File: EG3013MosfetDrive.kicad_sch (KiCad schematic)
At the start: 32 parts, among them J1 Conn_02x03_Odd_Even, Q1 QM6006D, Q2 QM6006D, Q3 QM6006D, Q4 QM6006D, U1 EG3013, U2 EG3013

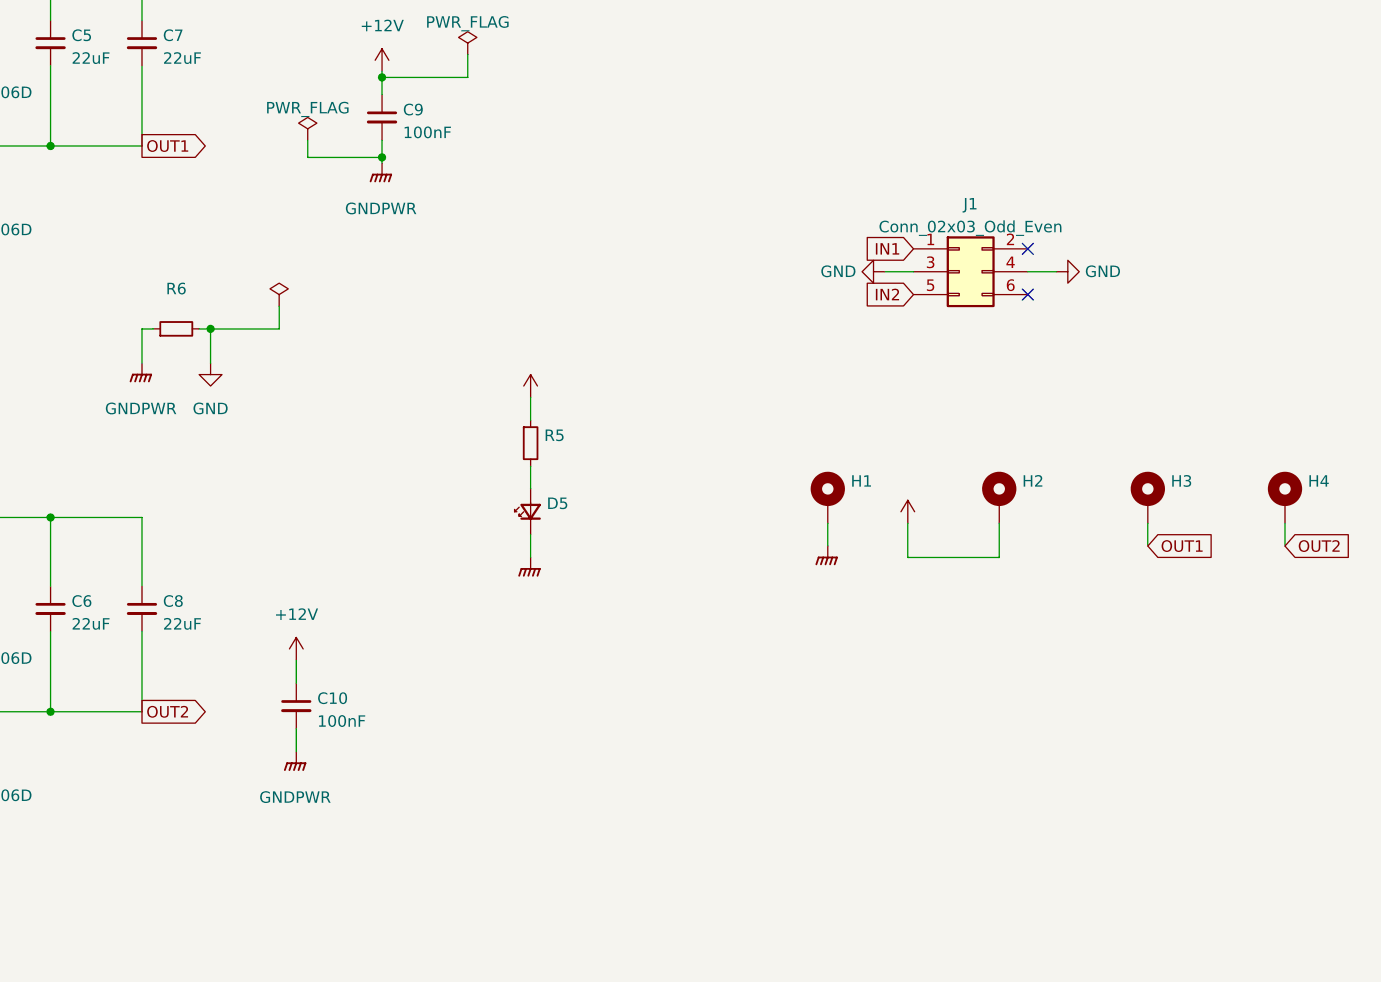
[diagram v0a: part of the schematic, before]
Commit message: PWM端口添加下拉电阻
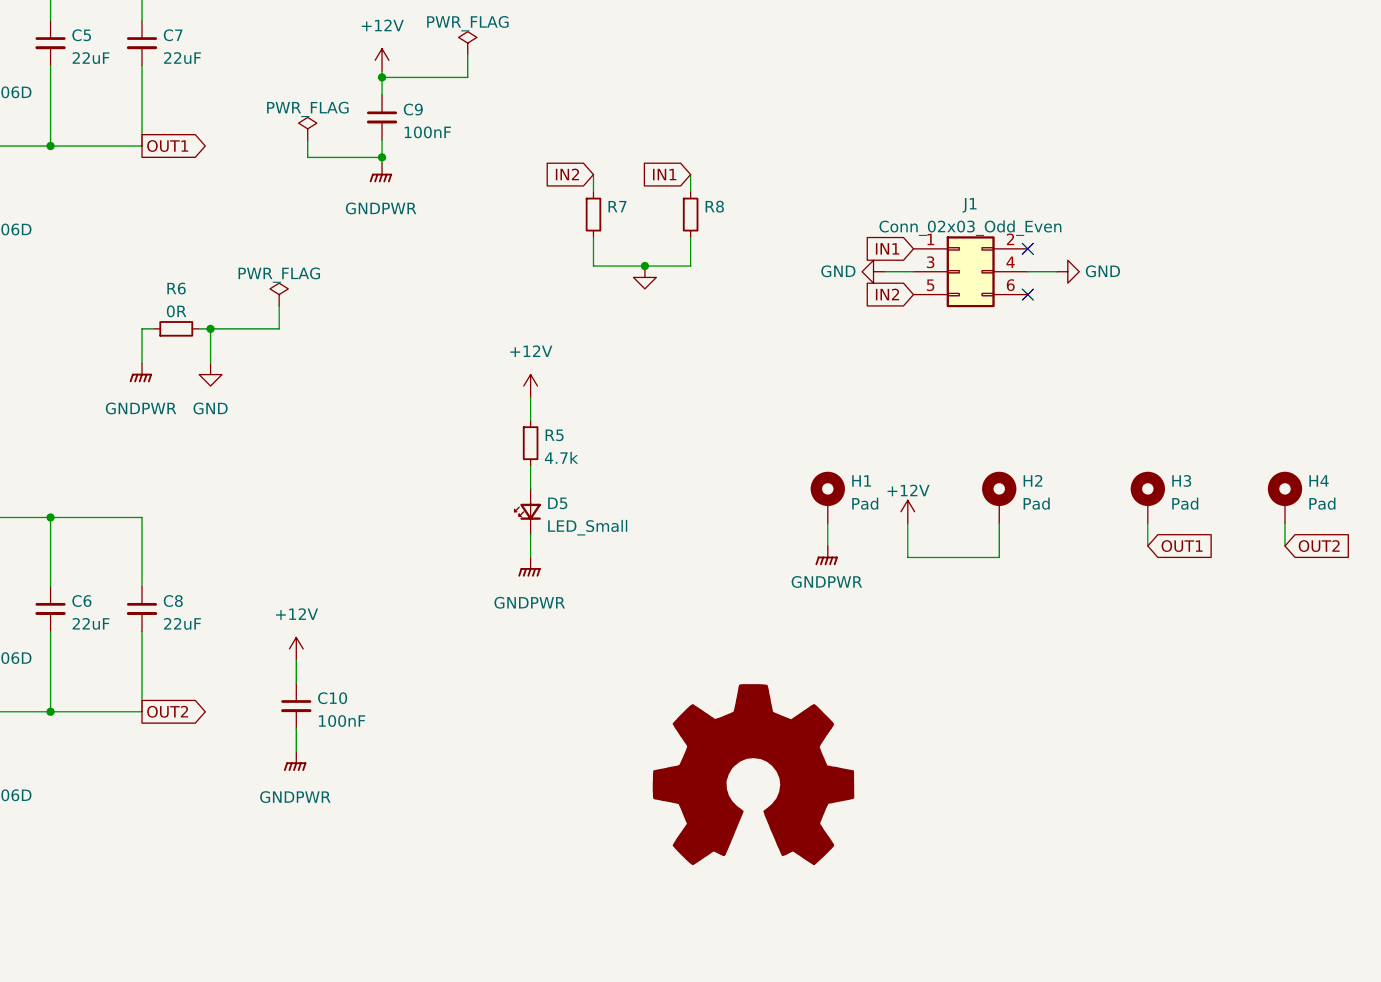
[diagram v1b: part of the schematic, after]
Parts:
- added R7, R8: (no value), symbol Device:R_Small
- D5: value (none) -> LED_Small; footprint (none) -> LED_SMD:LED_0402_1005Metric
- H1, H2, H3, H4: value (none) -> Pad; footprint (none) -> MountingHole:MountingHole_2.5mm_Pad_Via
- J1: footprint (none) -> Connector_IDC:IDC-Header_2x03_P2.54mm_Vertical
- R5: value (none) -> 4.7k; footprint (none) -> Resistor_SMD:R_0402_1005Metric
- R6: value (none) -> 0R; footprint (none) -> Resistor_SMD:R_0603_1608Metric
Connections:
- net GND: now also R7.2, R8.2
- net IN1: now also R8.1
- net IN2: now also R7.1

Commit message: fix some net
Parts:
- R7, R8: value (none) -> 1k; footprint (none) -> Resistor_SMD:R_0402_1005Metric
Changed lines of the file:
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@@
       (effects (font (size 1.27 1.27)) hide)
     )
-    (property "Value" "" (id 1) (at 188.595 154.94 0)
+    (property "Value" "Logo_Open_Hardware_Large" (id 1) (at 188.595 154.94 0)
       (effects (font (size 1.27 1.27)) hide)
     )
@@
       (effects (font (size 1.27 1.27)) (justify left))
     )
-    (property "Value" "" (id 1) (at 172.3136 82.9822 0)
-      (effects (font (size 1.27 1.27)) (justify left))
-    )
-    (property "Footprint" "" (id 2) (at 170.815 81.28 0)
+    (property "Value" "1k" (id 1) (at 172.3136 82.9822 0)
+      (effects (font (size 1.27 1.27)) (justify left))
+    )
+    (property "Footprint" "Resistor_SMD:R_0402_1005Metric" (id 2) (at 170.815 81.28 0)
       (effects (font (size 1.27 1.27)) hide)
     )
@@
       (effects (font (size 1.27 1.27)) hide)
     )
-    (property "Value" "" (id 1) (at 178.435 88.6988 0)
+    (property "Value" "GND" (id 1) (at 178.435 88.6988 0)
       (effects (font (size 1.27 1.27)) (justify left))
     )
@@
       (effects (font (size 1.27 1.27)) (justify left))
     )
-    (property "Value" "" (id 1) (at 183.1086 82.9822 0)
-      (effects (font (size 1.27 1.27)) (justify left))
-    )
-    (property "Footprint" "" (id 2) (at 181.61 81.28 0)
-      (effects (font (size 1.27 1.27)) hide)
-    )
+    (property "Value" "1k" (id 1) (at 183.1086 82.9822 0)
+      (effects (font (size 1.27 1.27)) (justify left))
+    )
+    (property "Footprint" "Resistor_SMD:R_0402_1005Metric" (id 2) (at 181.61 81.28 0)
+      (effects (font (size 1.27 1.27)) hide)
+    )

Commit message: model D Vesion
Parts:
- added C11, C12: 100nF, Capacitor_SMD:C_0603_1608Metric, symbol Device:C_Small
- added C13, C14, C15, C16: 10nF, Capacitor_SMD:C_0402_1005Metric, symbol Device:C_Small
- added C17, C18, C19, C20: 22uF, Capacitor_SMD:C_0603_1608Metric, symbol Device:C_Small
- added D6, D7, D8, D9: 1N4148, Diode_SMD:D_SOD-123, symbol Device:D_Small
- added H3, H6: Pad, MountingHole:MountingHole_2.5mm_Pad_Via, symbol Mechanical:MountingHole_Pad
- added Q5, Q6, Q7, Q8: QM6006D, Package_TO_SOT_SMD:TO-252-2, symbol Transistor_FET:QM6006D
- added R10, R9: 1k, Resistor_SMD:R_0402_1005Metric, symbol Device:R_Small
- added R11, R12, R13, R14: 22R, Resistor_SMD:R_0402_1005Metric, symbol Device:R_Small
- added U3, U4: EG3013, Package_SO:SOIC-8_3.9x4.9mm_P1.27mm, symbol Driver_FET:IR2103
- renumbered C10 to C1, C8 to C10, C9 to C2, C1 to C3, C2 to C4, C3 to C5, C4 to C6, C5 to C7, C6 to C8, C7 to C9, D5 to D1, D1 to D2, D2 to D3, D3 to D4, D4 to D5, H3 to H2, H2 to H4, H4 to H5, R6 to R1, R5 to R2, R1 to R3, R2 to R4, R3 to R5, R4 to R6
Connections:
- net +12V: now also C11.1, C12.1, Q5.2 (D), Q7.2 (D), U3.1 (VCC), U4.1 (VCC)
- net GND: now also R10.2, R9.2
- net GNDPWR: now also C11.2, C12.2, C14.1, C16.1, Q6.3 (S), Q8.3 (S), U3.4 (COM), U4.4 (COM)
- net IN2: now also U3.2 (HIN), U3.3 (~{LIN}); no longer U2.2 (HIN), U2.3 (~{LIN})
- net OUT2: now also C13.1, C17.2, C19.2, Q5.3 (S), Q6.2 (D), U3.6 (VS); no longer C10.2, C5.1, C8.2, Q3.3 (S), Q4.2 (D), U2.6 (VS)
- net IN3: now reaches J1.2 (Pin_2)
- net IN3: now also U2.2 (HIN), U2.3 (~{LIN}), R9.1
- net IN4: now reaches J1.6 (Pin_6)
- net IN4: now also R10.1, U4.2 (HIN), U4.3 (~{LIN})
- new net: D6.1 (K), R11.2, U3.7 (HO)
- new net: C13.2, D6.2 (A), Q5.1 (G), R11.1
- new net: C15.2, D8.2 (A), Q7.1 (G), R13.1
- new net: C18.1, C20.1, U4.8 (VB)
- new net: C17.1, C19.1, U3.8 (VB)
- new net: C14.2, D7.2 (A), Q6.1 (G), R12.1
- new net: D8.1 (K), R13.2, U4.7 (HO)
- new net: D7.1 (K), R12.2, U3.5 (LO)
- new net: C16.2, D9.2 (A), Q8.1 (G), R14.1
- new net: D9.1 (K), R14.2, U4.5 (LO)
- new net OUT3: C10.2, C5.1, C8.2, H3.1, Q3.3 (S), Q4.2 (D), U2.6 (VS)
- new net OUT4: C15.1, C18.2, C20.2, H6.1, Q7.3 (S), Q8.2 (D), U4.6 (VS)
- no-connect marks 2 -> 0
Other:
- note added: "此处实际没找到22uF的电容， 板子上装的是8uF的，芯片手 册上是这个位置47uF电容"
- title: B车模电机驱动 -> D车模电机驱动
- moved on the sheet: C1, C10, C2, C3, C4, C5, C6, C7, C8, C9, D1, D2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
